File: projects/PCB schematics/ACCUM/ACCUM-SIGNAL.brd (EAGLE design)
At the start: 57.1 x 58.1 mm, 23 parts, among them J1 2P(90DEG)_1-770966-0, J2 2P(90DEG)_1-770966-0, J3 2P(90DEG)_1-770966-0, J4 2P(90DEG)_1-770966-0, J5 2P(90DEG)_1-770966-0, Q1 IRFZ44Z

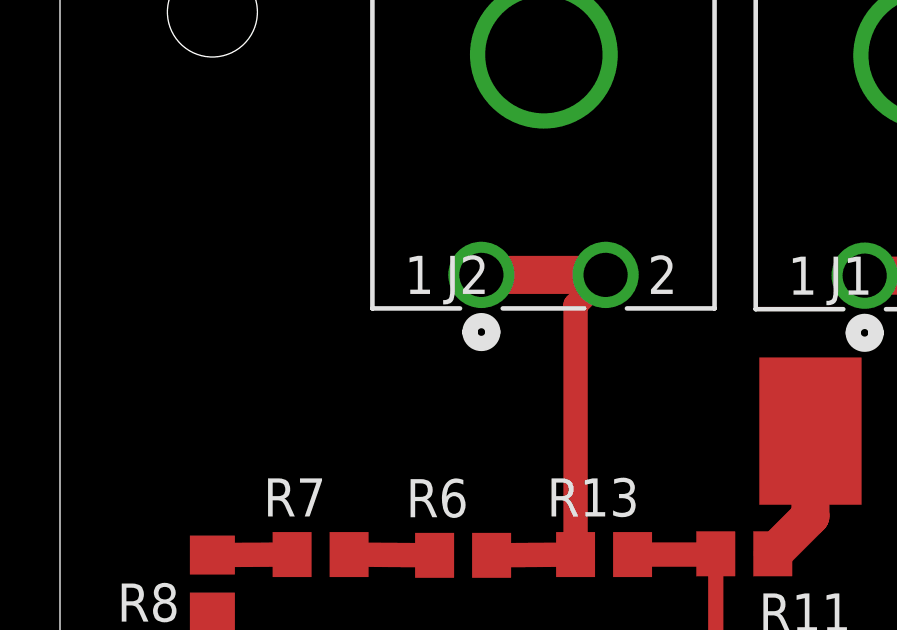
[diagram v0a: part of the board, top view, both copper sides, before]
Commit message: POWER - DCDC changes w/ Ryan.
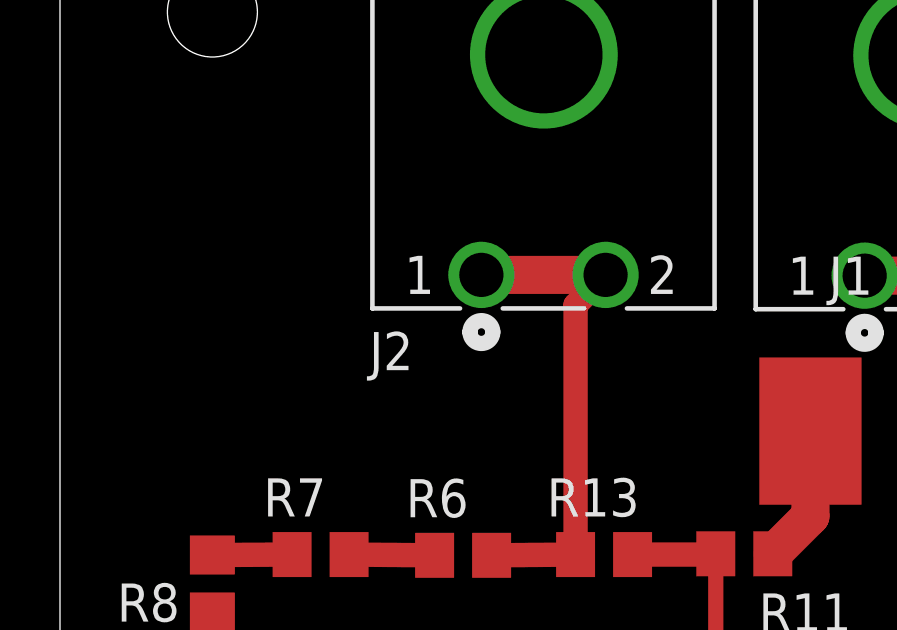
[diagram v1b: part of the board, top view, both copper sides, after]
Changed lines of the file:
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@@
 <layer number="42" name="bRestrict" color="1" fill="10" visible="no" active="yes"/>
 <layer number="43" name="vRestrict" color="2" fill="10" visible="no" active="yes"/>
-<layer number="44" name="Drills" color="7" fill="1" visible="no" active="yes"/>
-<layer number="45" name="Holes" color="7" fill="1" visible="no" active="yes"/>
+<layer number="44" name="Drills" color="7" fill="1" visible="yes" active="yes"/>
+<layer number="45" name="Holes" color="7" fill="1" visible="yes" active="yes"/>
 <layer number="46" name="Milling" color="3" fill="1" visible="no" active="yes"/>
 <layer number="47" name="Measures" color="7" fill="1" visible="no" active="yes"/>
@@
 <element name="J2" library="con-MATE-N-LOK" package="CON2_1X2_P163_RAMNL" value="2P(90DEG)_1-770966-0" x="18.1864" y="44.577" smashed="yes">
 <attribute name="MANUFACTURER_PART_NUMBER" value="17709660" x="18.1864" y="44.577" size="1.778" layer="27" display="off"/>
-<attribute name="NAME" x="12.8524" y="43.942" size="1.27" layer="25" ratio="6" rot="SR0"/>
+<attribute name="NAME" x="10.3124" y="41.402" size="1.27" layer="25" ratio="6" rot="SR0"/>
 <attribute name="VENDOR" value="TE Connectivity" x="18.1864" y="44.577" size="1.778" layer="27" display="off"/>
 </element>

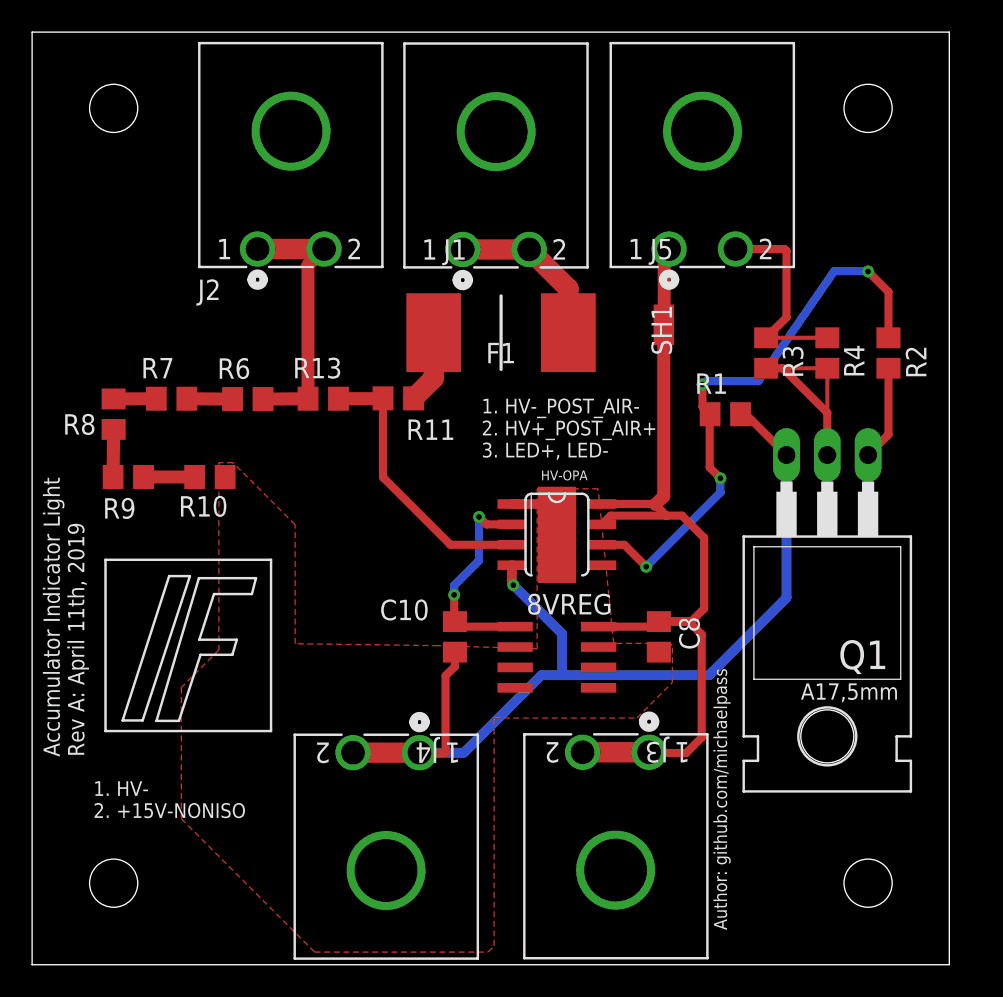
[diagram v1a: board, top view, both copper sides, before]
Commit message: PROJ - Silkscreen modifications - 50%.
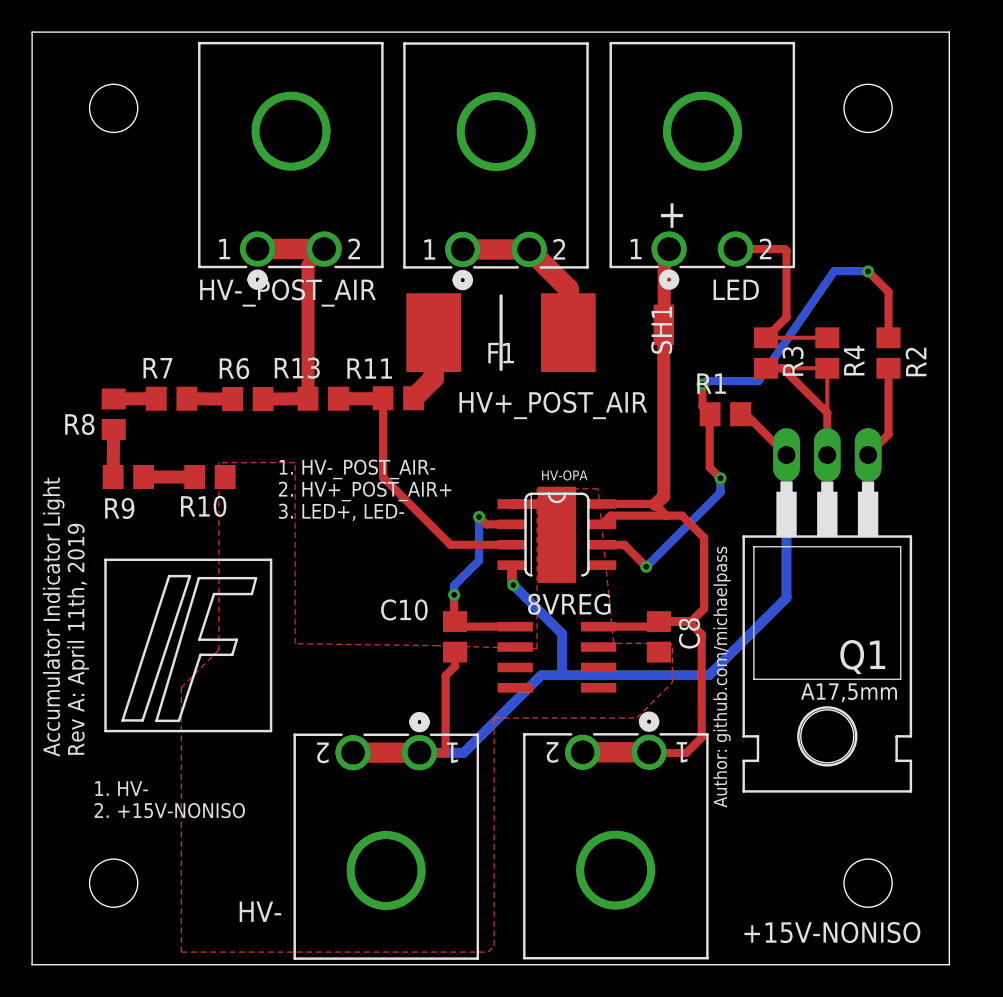
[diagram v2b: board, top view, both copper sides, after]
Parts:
- renumbered J1 to HV+_POST_AIR, J2 to HV-_POST_AIR, J3 to +15V-NONISO, J4 to HV-, J5 to LED
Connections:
- net HV+_POST_AIR+ renamed HV+_POST_AIR
- net HV-_POST_AIR- renamed HV-_POST_AIR
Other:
- board text added: "+"
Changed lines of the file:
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@@
 <text x="3.2512" y="12.954" size="1.016" layer="25" font="vector" rot="R90">Accumulator Indicator Light
 Rev A: April 11th, 2019</text>
-<text x="43.2816" y="2.159" size="0.8128" layer="25" font="vector" rot="R90">Author: github.com/michaelpass</text>
+<text x="43.2816" y="9.779" size="0.8128" layer="25" font="vector" rot="R90">Author: github.com/michaelpass</text>
 <text x="3.81" y="9.144" size="0.9144" layer="25" font="vector">1. HV-
 2. +15V-NONISO</text>
@@
 <wire x1="13.6906" y1="23.0886" x2="13.9446" y2="24.0792" width="0.1524" layer="25"/>
 <wire x1="13.9446" y1="24.0792" x2="10.3886" y2="24.0792" width="0.1524" layer="25"/>
-<text x="27.9908" y="31.5976" size="0.9144" layer="25" font="vector">1. HV-_POST_AIR-
+<text x="15.2908" y="27.7876" size="0.9144" layer="25" font="vector">1. HV-_POST_AIR-
 2. HV+_POST_AIR+
 3. LED+, LED-</text>
+<text x="38.9382" y="45.8978" size="1.778" layer="21">+</text>
 </plain>
 <attributes>
@@
 </element>
 <element name="R11" library="rcl" library_urn="urn:adsk.eagle:library:334" package="R0805" package3d_urn="urn:adsk.eagle:package:23553/2" value="680k" x="22.8092" y="35.2806" smashed="yes">
-<attribute name="NAME" x="23.2918" y="32.6898" size="1.27" layer="25"/>
+<attribute name="NAME" x="19.4818" y="36.4998" size="1.27" layer="25"/>
 <attribute name="SPICEPREFIX" value="R" x="10.1092" y="72.1106" size="1.778" layer="27" display="off"/>
 </element>
 <element name="R13" library="rcl" library_urn="urn:adsk.eagle:library:334" package="R0805" package3d_urn="urn:adsk.eagle:package:23553/2" value="120k" x="18.1356" y="35.2552" smashed="yes">
-<attribute name="NAME" x="16.2306" y="36.5252" size="1.27" layer="25"/>
+<attribute name="NAME" x="14.9606" y="36.5252" size="1.27" layer="25"/>
 <attribute name="SPICEPREFIX" value="R" x="-0.9144" y="65.7352" size="1.778" layer="27" display="off"/>
 </element>
@@
 <attribute name="SPICEPREFIX" value="C" x="37.7698" y="36.9316" size="1.778" layer="27" rot="R270" display="off"/>
 </element>
-<element name="J1" library="con-MATE-N-LOK" package="CON2_1X2_P163_RAMNL" value="2P(90DEG)_1-770966-0" x="30.9626" y="44.5516" smashed="yes">
+<element name="HV+_POST_AIR" library="con-MATE-N-LOK" package="CON2_1X2_P163_RAMNL" value="2P(90DEG)_1-770966-0" x="30.9626" y="44.5516" smashed="yes">
 <attribute name="MANUFACTURER_PART_NUMBER" value="17709660" x="30.9626" y="44.5516" size="1.778" layer="27" display="off"/>
-<attribute name="NAME" x="25.6286" y="43.9166" size="1.27" layer="25" ratio="6" rot="SR0"/>
+<attribute name="NAME" x="26.4668" y="34.3916" size="1.27" layer="25" ratio="6" rot="SR0"/>
 <attribute name="VENDOR" value="TE Connectivity" x="30.9626" y="44.5516" size="1.778" layer="27" display="off"/>
 </element>
-<element name="J2" library="con-MATE-N-LOK" package="CON2_1X2_P163_RAMNL" value="2P(90DEG)_1-770966-0" x="18.1864" y="44.577" smashed="yes">
+<element name="HV-_POST_AIR" library="con-MATE-N-LOK" package="CON2_1X2_P163_RAMNL" value="2P(90DEG)_1-770966-0" x="18.1864" y="44.577" smashed="yes">
 <attribute name="MANUFACTURER_PART_NUMBER" value="17709660" x="18.1864" y="44.577" size="1.778" layer="27" display="off"/>
 <attribute name="NAME" x="10.3124" y="41.402" size="1.27" layer="25" ratio="6" rot="SR0"/>
 <attribute name="VENDOR" value="TE Connectivity" x="18.1864" y="44.577" size="1.778" layer="27" display="off"/>
 </element>
-<element name="J4" library="con-MATE-N-LOK" package="CON2_1X2_P163_RAMNL" value="2P(90DEG)_1-770966-0" x="19.9898" y="13.208" smashed="yes" rot="R180">
+<element name="HV-" library="con-MATE-N-LOK" package="CON2_1X2_P163_RAMNL" value="2P(90DEG)_1-770966-0" x="19.9898" y="13.208" smashed="yes" rot="R180">
 <attribute name="MANUFACTURER_PART_NUMBER" value="17709660" x="19.9898" y="13.208" size="1.778" layer="27" rot="R180" display="off"/>
-<attribute name="NAME" x="25.3238" y="13.843" size="1.27" layer="25" ratio="6" rot="SR180"/>
+<attribute name="NAME" x="12.7762" y="2.667" size="1.27" layer="25" ratio="6" rot="SR0"/>
 <attribute name="VENDOR" value="TE Connectivity" x="19.9898" y="13.208" size="1.778" layer="27" rot="R180" display="off"/>
 </element>
-<element name="J3" library="con-MATE-N-LOK" package="CON2_1X2_P163_RAMNL" value="2P(90DEG)_1-770966-0" x="34.29" y="13.2334" smashed="yes" rot="R180">
+<element name="+15V-NONISO" library="con-MATE-N-LOK" package="CON2_1X2_P163_RAMNL" value="2P(90DEG)_1-770966-0" x="34.29" y="13.2334" smashed="yes" rot="R180">
 <attribute name="MANUFACTURER_PART_NUMBER" value="17709660" x="48.26" y="-3.2766" size="1.778" layer="27" rot="R180" display="off"/>
-<attribute name="NAME" x="39.624" y="13.8684" size="1.27" layer="25" ratio="6" rot="SR180"/>
+<attribute name="NAME" x="44.196" y="1.3716" size="1.27" layer="25" ratio="6" rot="SR0"/>
 <attribute name="VENDOR" value="TE Connectivity" x="48.26" y="-3.2766" size="1.778" layer="27" rot="R180" display="off"/>
 </element>
-<element name="J5" library="con-MATE-N-LOK" package="CON2_1X2_P163_RAMNL" value="2P(90DEG)_1-770966-0" x="43.815" y="44.577" smashed="yes">
+<element name="LED" library="con-MATE-N-LOK" package="CON2_1X2_P163_RAMNL" value="2P(90DEG)_1-770966-0" x="43.815" y="44.577" smashed="yes">
 <attribute name="MANUFACTURER_PART_NUMBER" value="17709660" x="29.845" y="61.087" size="1.778" layer="27" display="off"/>
-<attribute name="NAME" x="38.481" y="43.942" size="1.27" layer="25" ratio="6" rot="SR0"/>
+<attribute name="NAME" x="42.291" y="41.402" size="1.27" layer="25" ratio="6" rot="SR0"/>
 <attribute name="VENDOR" value="TE Connectivity" x="29.845" y="61.087" size="1.778" layer="27" display="off"/>
 </element>
@@
 <contactref element="C10" pad="2"/>
 <contactref element="C8" pad="2"/>
-<contactref element="J4" pad="1"/>
-<contactref element="J4" pad="2"/>
+<contactref element="HV-" pad="1"/>
+<contactref element="HV-" pad="2"/>
 <contactref element="HV-OPA" pad="THERMAL"/>
 <wire x1="19.9898" y1="13.208" x2="24.13" y2="13.208" width="1.27" layer="1"/>
@@
 <vertex x="25.288828125" y="19.872371875"/>
 <vertex x="16.383" y="19.994771875"/>
-<vertex x="16.383" y="27.4066"/>
-<vertex x="12.51574375" y="31.27385625"/>
+<vertex x="16.383" y="31.27385625"/>
 <vertex x="11.6332" y="31.27385625"/>
 <vertex x="11.6332" y="19.6088"/>
 <vertex x="9.2964" y="17.272"/>
-<vertex x="9.2964" y="9.0932"/>
-<vertex x="17.6022" y="0.7874"/>
+<vertex x="9.2964" y="0.7874"/>
 <vertex x="28.3972" y="0.7874"/>
 <vertex x="28.7782" y="1.1684"/>
@@
 <wire x1="26.0604" y1="26.1566" x2="29.8898" y2="26.1566" width="0.508" layer="1"/>
 </signal>
-<signal name="HV+_POST_AIR+">
-<contactref element="J1" pad="1"/>
-<contactref element="J1" pad="2"/>
+<signal name="HV+_POST_AIR">
+<contactref element="HV+_POST_AIR" pad="1"/>
+<contactref element="HV+_POST_AIR" pad="2"/>
 <wire x1="26.8224" y1="44.5516" x2="30.9626" y2="44.5516" width="1.27" layer="1"/>
 <wire x1="26.7716" y1="44.5516" x2="26.8224" y2="44.5516" width="0.8128" layer="1"/>
@@
 <contactref element="8VREG" pad="8"/>
 <contactref element="C8" pad="1"/>
-<contactref element="J3" pad="1"/>
-<contactref element="J3" pad="2"/>
+<contactref element="+15V-NONISO" pad="1"/>
+<contactref element="+15V-NONISO" pad="2"/>
 <wire x1="34.29" y1="13.2334" x2="38.4302" y2="13.2334" width="1.27" layer="1"/>
 <wire x1="35.2898" y1="21.0566" x2="38.7248" y2="21.0566" width="0.508" layer="1"/>
@@
 <wire x1="38.8239" y1="28.6639" x2="39.3446" y2="29.1846" width="0.8128" layer="1"/>
 </signal>
-<signal name="HV-_POST_AIR-">
+<signal name="HV-_POST_AIR">
 <contactref element="R13" pad="1"/>
 <contactref element="R6" pad="1"/>
-<contactref element="J2" pad="1"/>
-<contactref element="J2" pad="2"/>
+<contactref element="HV-_POST_AIR" pad="1"/>
+<contactref element="HV-_POST_AIR" pad="2"/>
 <wire x1="14.0462" y1="44.577" x2="18.1864" y2="44.577" width="1.27" layer="1"/>
 <wire x1="14.3866" y1="35.2298" x2="17.1856" y2="35.2552" width="0.8128" layer="1"/>
@@
 </signal>
 <signal name="LED+">
-<contactref element="J5" pad="1"/>
+<contactref element="LED" pad="1"/>
 <contactref element="SH1" pad="2"/>
 <wire x1="39.6748" y1="44.577" x2="39.37" y2="44.2722" width="0.8128" layer="1"/>
@@
 </signal>
 <signal name="LED-">
-<contactref element="J5" pad="2"/>
+<contactref element="LED" pad="2"/>
 <contactref element="R3" pad="1"/>
 <wire x1="46.99" y1="44.45" x2="46.99" y2="40.32" width="0.508" layer="1"/>

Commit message: PROJ - Gerber files major milestone - 05/05/19.
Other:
- board text added: "Accumulator Indicator Light Rev A: May 5th, 2019"
- board text removed: "Accumulator Indicator Light Rev A: April 11th, 2019"
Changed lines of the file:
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@@
 <hole x="5.08" y="5.08" drill="3"/>
 <text x="3.2512" y="12.954" size="1.016" layer="25" font="vector" rot="R90">Accumulator Indicator Light
-Rev A: April 11th, 2019</text>
+Rev A: May 5th, 2019</text>
 <text x="43.2816" y="9.779" size="0.8128" layer="25" font="vector" rot="R90">Author: github.com/michaelpass</text>
 <text x="3.81" y="9.144" size="0.9144" layer="25" font="vector">1. HV-
@@
 <contactref element="HV+_POST_AIR" pad="2"/>
 <wire x1="26.8224" y1="44.5516" x2="30.9626" y2="44.5516" width="1.27" layer="1"/>
-<wire x1="26.7716" y1="44.5516" x2="26.8224" y2="44.5516" width="0.8128" layer="1"/>
 <contactref element="F1" pad="1"/>
 <wire x1="30.9626" y1="44.5516" x2="33.405" y2="42.1092" width="1.27" layer="1"/>
